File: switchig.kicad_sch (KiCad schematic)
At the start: 0 parts

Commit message: Symbols and references for the switcher squematic
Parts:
- added D?: DF005s, Diode_THT:Diode_Bridge_DIP-4_W7.62mm_P5.08mm, symbol Diode_Bridge:DF005M
- added D?: DF206S-G, Diode_THT:Diode_Bridge_DIP-4_W7.62mm_P5.08mm, symbol Diode_Bridge:DF005M
- added Q? (x2): ~, symbol TeslaCoil:STGB19NC60KDT4
- added U?: ~, symbol TeslaCoil:SN74LVC2G14-Q1
- added U?: 7815L, symbol Regulator_Linear:L7815
- added U?: 78L05Z, symbol Regulator_Linear:L7815
- added U? (x2): ~, symbol TeslaCoil:UCC27425
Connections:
- new net: U?.1 (ENBA), U?.1 (ENBA)
- new net: U?.2 (INA), U?.2 (INA)
- new net: U?.3 (GND), U?.3 (GND)
- new net: U?.4 (INB), U?.4 (INB)
- new net: U?.5 (OUTB), U?.5 (OUTB)
- new net: U?.6 (VCC), U?.6 (VCC)
- new net: U?.7 (OUTA), U?.7 (OUTA)
- new net: U?.8 (ENBB), U?.8 (ENBB)
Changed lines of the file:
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@@
     (comment 2 "Juan Felipe Osorio Franco")
   )
+  (symbol (lib_id "Diode_Bridge:DF005M") (at 78.74 60.96 0) (unit 1)
+    (in_bom yes) (on_board yes) (dnp no)
+    (property "Reference" "D?" (at 86.36 53.34 0)
+      (effects (font (size 1.27 1.27)))
+    )
+    (property "Value" "DF005s" (at 86.36 55.88 0)
+      (effects (font (size 1.27 1.27)))
+    )
+    (property "Footprint" "Diode_THT:Diode_Bridge_DIP-4_W7.62mm_P5.08mm" (at 82.55 57.785 0)
+      (effects (font (size 1.27 1.27)) (justify left) hide)
+    )
+    (property "Datasheet" "http://www.vishay.com/docs/88571/dfm.pdf" (at 78.74 60.96 0)
+      (effects (font (size 1.27 1.27)) hide)
+    )
+    (pin "1")
+    (pin "2")
+    (pin "3")
+    (pin "4")
+    (instances
+      (project "TeslaCoil"
+        (path "/d01f06f4-4cef-4772-977e-9df687e0dd50/8a45e165-3ed3-49a9-9619-ad3a4fdbe0cf"
+          (reference "D?") (unit 1)
+        )
+      )
+    )
+  )
+  (symbol (lib_id "Diode_Bridge:DF005M") (at 78.74 80.01 0) (unit 1)
+    (in_bom yes) (on_board yes) (dnp no)
+    (property "Reference" "D?" (at 86.36 72.39 0)
+      (effects (font (size 1.27 1.27)))
+    )
+    (property "Value" "DF206S-G" (at 86.36 74.93 0)
+      (effects (font (size 1.27 1.27)))
+    )
+    (property "Footprint" "Diode_THT:Diode_Bridge_DIP-4_W7.62mm_P5.08mm" (at 82.55 76.835 0)
+      (effects (font (size 1.27 1.27)) (justify left) hide)
+    )
+    (property "Datasheet" "http://www.vishay.com/docs/88571/dfm.pdf" (at 78.74 80.01 0)
+      (effects (font (size 1.27 1.27)) hide)
+    )
+    (pin "1")
+    (pin "2")
+    (pin "3")
+    (pin "4")
+    (instances
+      (project "TeslaCoil"
+        (path "/d01f06f4-4cef-4772-977e-9df687e0dd50/8a45e165-3ed3-49a9-9619-ad3a4fdbe0cf"
+          (reference "D?") (unit 1)
+        )
+      )
+    )
+  )
+  (symbol (lib_id "TeslaCoil:STGB19NC60KDT4") (at 154.94 49.53 0) (unit 1)
+    (in_bom yes) (on_board yes) (dnp no) (fields_autoplaced)
+    (property "Reference" "Q?" (at 160.02 49.53 0)
+      (effects (font (size 1.27 1.27)) (justify left))
+    )
+    (property "Value" "~" (at 157.48 49.53 0)
+      (effects (font (size 1.27 1.27)))
+    )
+    (property "Footprint" "" (at 157.48 49.53 0)
+      (effects (font (size 1.27 1.27)) hide)
+    )
+    (property "Datasheet" "" (at 157.48 49.53 0)
+      (effects (font (size 1.27 1.27)) hide)
+    )
+    (pin "1")
+    (pin "2")
+    (pin "3")
+    (instances
+      (project "TeslaCoil"
+        (path "/d01f06f4-4cef-4772-977e-9df687e0dd50/8a45e165-3ed3-49a9-9619-ad3a4fdbe0cf"
+          (reference "Q?") (unit 1)
+        )
+      )
+    )
+  )
+  (symbol (lib_id "TeslaCoil:STGB19NC60KDT4") (at 154.94 62.23 0) (unit 1)
+    (in_bom yes) (on_board yes) (dnp no) (fields_autoplaced)
+    (property "Reference" "Q?" (at 160.02 62.23 0)
+      (effects (font (size 1.27 1.27)) (justify left))
+    )
+    (property "Value" "~" (at 157.48 62.23 0)
+      (effects (font (size 1.27 1.27)))
+    )
+    (property "Footprint" "" (at 157.48 62.23 0)
+      (effects (font (size 1.27 1.27)) hide)
+    )
+    (property "Datasheet" "" (at 157.48 62.23 0)
+      (effects (font (size 1.27 1.27)) hide)
+    )
+    (pin "1")
+    (pin "2")
+    (pin "3")
+    (instances
+      (project "TeslaCoil"
+        (path "/d01f06f4-4cef-4772-977e-9df687e0dd50/8a45e165-3ed3-49a9-9619-ad3a4fdbe0cf"
+          (reference "Q?") (unit 1)
+        )
+      )
+    )
+  )
+  (symbol (lib_id "TeslaCoil:SN74LVC2G14-Q1") (at 132.08 55.88 0) (unit 1)
+    (in_bom yes) (on_board yes) (dnp no) (fields_autoplaced)
+    (property "Reference" "U?" (at 131.445 41.91 0)
+      (effects (font (size 1.27 1.27)))
+    )
+    (property "Value" "~" (at 133.35 45.72 0)
+      (effects (font (size 1.27 1.27)))
+    )
+    (property "Footprint" "" (at 133.35 45.72 0)
+      (effects (font (size 1.27 1.27)) hide)
+    )
+    (property "Datasheet" "" (at 133.35 45.72 0)
+      (effects (font (size 1.27 1.27)) hide)
+    )
+    (pin "1")
+    (pin "2")
+    (pin "3")
+    (pin "4")
+    (pin "5")
+    (pin "6")
+    (instances
+      (project "TeslaCoil"
+        (path "/d01f06f4-4cef-4772-977e-9df687e0dd50/8a45e165-3ed3-49a9-9619-ad3a4fdbe0cf"
+          (reference "U?") (unit 1)
+        )
+      )
+    )
+  )
+  (symbol (lib_id "Regulator_Linear:L7815") (at 101.6 59.69 0) (unit 1)
+    (in_bom yes) (on_board yes) (dnp no) (fields_autoplaced)
+    (property "Reference" "U?" (at 101.6 53.34 0)
+      (effects (font (size 1.27 1.27)))
+    )
+    (property "Value" "7815L" (at 101.6 55.88 0)
+      (effects (font (size 1.27 1.27)))
+    )
+    (property "Footprint" "" (at 102.235 63.5 0)
+      (effects (font (size 1.27 1.27) italic) (justify left) hide)
+    )
+    (property "Datasheet" "http://www.st.com/content/ccc/resource/technical/document/datasheet/41/4f/b3/b0/12/d4/47/88/CD00000444.pdf/files/CD00000444.pdf/jcr:content/translations/en.CD00000444.pdf" (at 101.6 60.96 0)
+      (effects (font (size 1.27 1.27)) hide)
+    )
+    (pin "1")
+    (pin "2")
+    (pin "3")
+    (instances
+      (project "TeslaCoil"
+        (path "/d01f06f4-4cef-4772-977e-9df687e0dd50/8a45e165-3ed3-49a9-9619-ad3a4fdbe0cf"
+          (reference "U?") (unit 1)
+        )
+      )
+    )
+  )
+  (symbol (lib_id "Regulator_Linear:L7815") (at 100.33 81.28 0) (unit 1)
+    (in_bom yes) (on_board yes) (dnp no) (fields_autoplaced)
+    (property "Reference" "U?" (at 100.33 74.93 0)
+      (effects (font (size 1.27 1.27)))
+    )
+    (property "Value" "78L05Z" (at 100.33 77.47 0)
+      (effects (font (size 1.27 1.27)))
+    )
+    (property "Footprint" "" (at 100.965 85.09 0)
+      (effects (font (size 1.27 1.27) italic) (justify left) hide)
+    )
+    (property "Datasheet" "http://www.st.com/content/ccc/resource/technical/document/datasheet/41/4f/b3/b0/12/d4/47/88/CD00000444.pdf/files/CD00000444.pdf/jcr:content/translations/en.CD00000444.pdf" (at 100.33 82.55 0)
+      (effects (font (size 1.27 1.27)) hide)
+    )
+    (pin "1")
+    (pin "2")
+    (pin "3")
+    (instances
+      (project "TeslaCoil"
+        (path "/d01f06f4-4cef-4772-977e-9df687e0dd50/8a45e165-3ed3-49a9-9619-ad3a4fdbe0cf"
+          (reference "U?") (unit 1)
+        )
+      )
+    )
+  )
+  (symbol (lib_id "TeslaCoil:UCC27425") (at 129.54 85.09 0) (unit 1)
+    (in_bom yes) (on_board yes) (dnp no) (fields_autoplaced)
+    (property "Reference" "U?" (at 128.905 71.12 0)
+      (effects (font (size 1.27 1.27)))
+    )
+    (property "Value" "~" (at 129.54 85.09 0)
+      (effects (font (size 1.27 1.27)))
+    )
+    (property "Footprint" "" (at 129.54 85.09 0)
+      (effects (font (size 1.27 1.27)) hide)
+    )
+    (property "Datasheet" "" (at 129.54 85.09 0)
+      (effects (font (size 1.27 1.27)) hide)
+    )
+    (pin "1")
+    (pin "2")
+    (pin "3")
+    (pin "4")
+    (pin "5")
+    (pin "6")
+    (pin "7")
+    (pin "8")
+    (instances
+      (project "TeslaCoil"
+        (path "/d01f06f4-4cef-4772-977e-9df687e0dd50/8a45e165-3ed3-49a9-9619-ad3a4fdbe0cf"
+          (reference "U?") (unit 1)
+        )
+      )
+    )
+  )
+  (symbol (lib_id "TeslaCoil:UCC27425") (at 129.54 85.09 0) (unit 1)
+    (in_bom yes) (on_board yes) (dnp no) (fields_autoplaced)
+    (property "Reference" "U?" (at 128.905 71.12 0)
+      (effects (font (size 1.27 1.27)))
+    )
+    (property "Value" "~" (at 129.54 85.09 0)
+      (effects (font (size 1.27 1.27)))
+    )
+    (property "Footprint" "" (at 129.54 85.09 0)
+      (effects (font (size 1.27 1.27)) hide)
+    )
+    (property "Datasheet" "" (at 129.54 85.09 0)
+      (effects (font (size 1.27 1.27)) hide)
+    )
+    (pin "1")
+    (pin "2")
+    (pin "3")
+    (pin "4")
+    (pin "5")
+    (pin "6")
+    (pin "7")
+    (pin "8")
+    (instances
+      (project "TeslaCoil"
+        (path "/d01f06f4-4cef-4772-977e-9df687e0dd50/8a45e165-3ed3-49a9-9619-ad3a4fdbe0cf"
+          (reference "U?") (unit 1)
+        )
+      )
+    )
+  )
 )

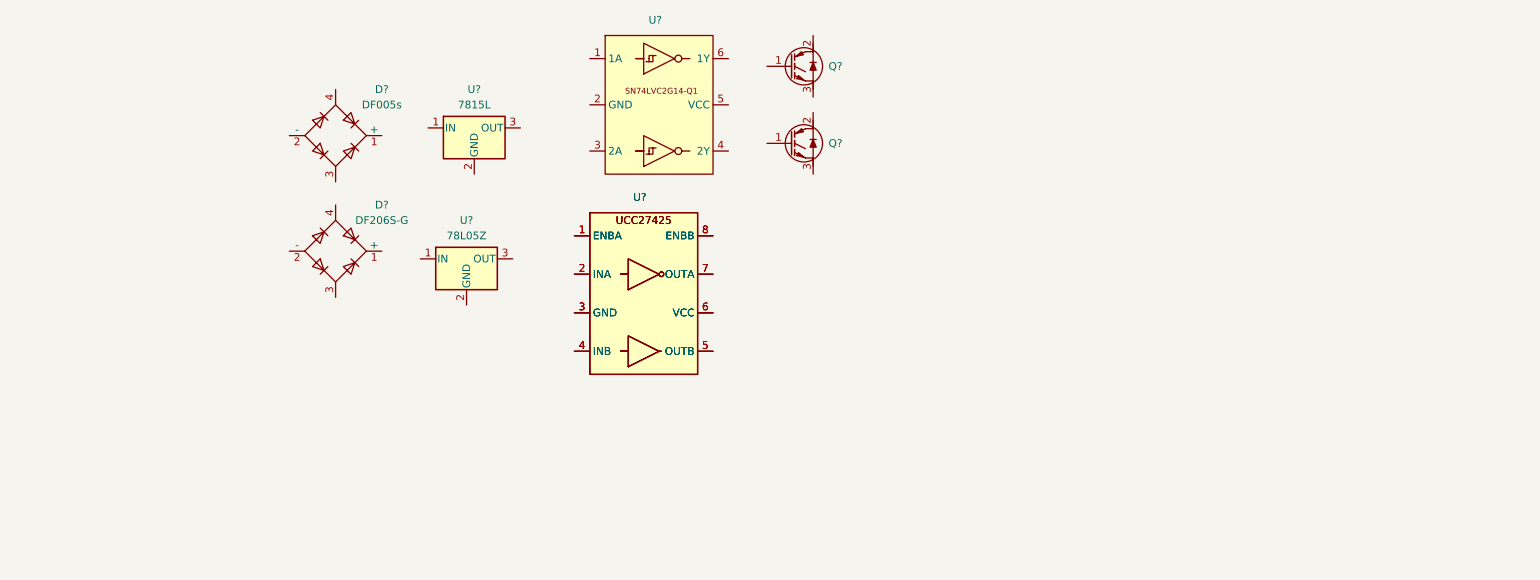
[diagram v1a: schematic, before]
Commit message: Finished switching circuit schematic, added txt file for component references
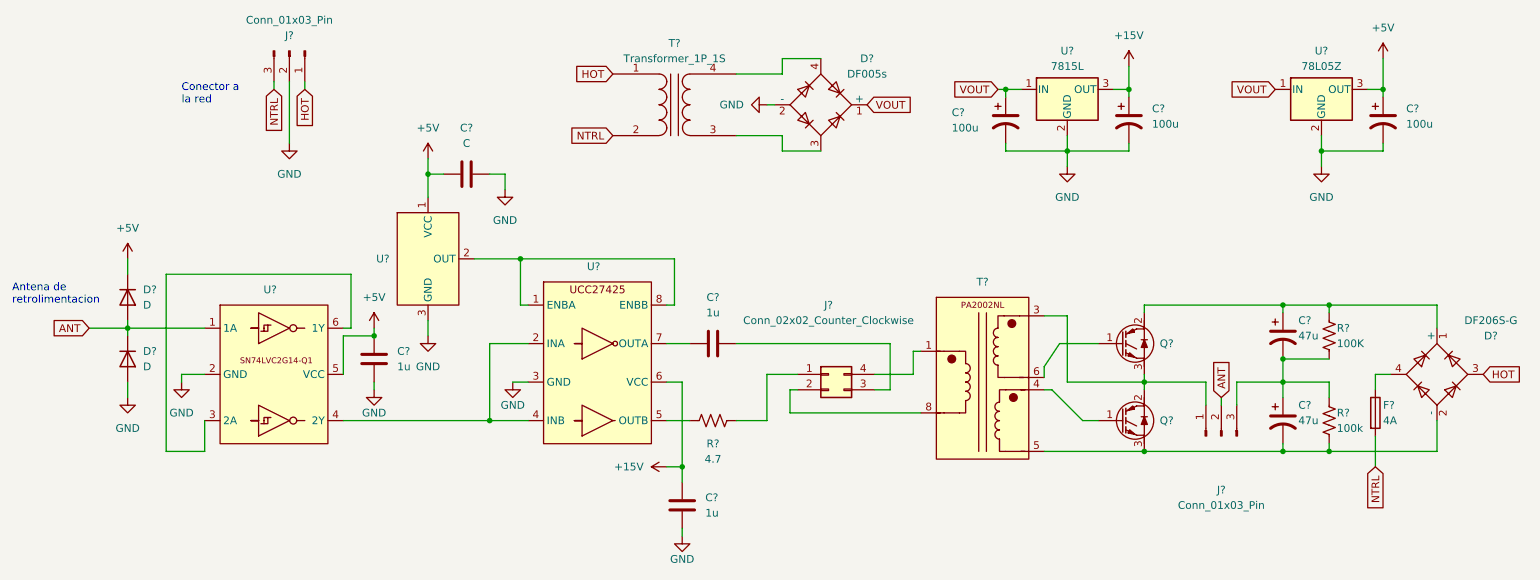
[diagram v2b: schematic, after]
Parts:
- removed U?: ~, symbol TeslaCoil:UCC27425
- added C? (x3): 1u, symbol Device:C
- added C? (x3): 100u, symbol Device:C_Polarized_US
- added C? (x2): 47u, symbol Device:C_Polarized_US
- added C?: C, symbol Device:C
- added D? (x2): D, symbol Device:D
- added F?: 4A, symbol Device:Fuse
- added J? (x2): Conn_01x03_Pin, symbol Connector:Conn_01x03_Pin
- added J?: Conn_02x02_Counter_Clockwise, symbol Connector_Generic:Conn_02x02_Counter_Clockwise
- added R?: 100k, symbol Device:R_US
- added R?: 4.7, symbol Device:R_US
- added R?: 100K, symbol Device:R_US
- added T?: ~, symbol TeslaCoil:PA2002NL
- added T?: Transformer_1P_1S, symbol Device:Transformer_1P_1S
- added U?: ~, symbol TeslaCoil:IF-D95T
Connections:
- net VOUT: now reaches D?.1 (+)
- net VOUT: now also U?.1 (IN), U?.1 (IN), C?.1
- net GND: now reaches D?.2 (-)
- net GND: now also U?.2 (GND), U?.2 (GND), U?.2 (GND), U?.3 (GND), C?.2, C?.2, C?.2, C?.2, C?.2, C?.2, D?.2 (A), J?.2 (Pin_2), U?.3 (GND)
- net at D?.3: now also T?.3 (SA)
- net at D?.4: now also T?.4 (SB)
- net at D?.1 (+): now also Q?.2, C?.1, R?.1
- net at D?.2 (-): now also Q?.3, C?.2, R?.2, T?.5
- net HOT: now reaches D?.3
- net HOT: now also J?.1 (Pin_1), T?.1 (AA)
- net at D?.4: now also F?.1
- net at Q?.1: now also T?.6
- net at Q?.3: now also Q?.2, J?.1 (Pin_1), T?.3
- net at Q?.1: now also T?.4
- net ANT: now reaches U?.1 (1A)
- net ANT: now also D?.1 (K), D?.2 (A), J?.2 (Pin_2)
- net at U?.3 (2A): now also U?.6 (1Y)
- net at U?.4 (2Y): now also U?.2 (INA), U?.4 (INB)
- net +5V: now reaches U?.5 (VCC)
- net +5V: now also U?.3 (OUT), C?.1, C?.1, C?.1, D?.1 (K), U?.1 (VCC)
- net +15V: now reaches U?.3 (OUT)
- net +15V: now also U?.6 (VCC), C?.1, C?.1
- net at U?.1 (ENBA): now also U?.8 (ENBB), U?.2 (OUT)
- net at U?.5 (OUTB): now also R?.1
- net at U?.7 (OUTA): now also C?.1
- new net: C?.2, J?.3 (Pin_3)
- new net: C?.1, C?.2, J?.3 (Pin_3), R?.1, R?.2
- new net: J?.4 (Pin_4), T?.1
- new net: J?.2 (Pin_2), T?.8
- new net: J?.1 (Pin_1), R?.2
- new net NTRL: F?.2, J?.3 (Pin_3), T?.2 (AB)
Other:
- note added: "Antena de retrolimentacion"
- note added: "Conector a la red"
- moved on the sheet: D?, Q?, U?
